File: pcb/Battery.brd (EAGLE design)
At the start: 90 x 15 mm, 18 parts, among them IC1 SN74LVC14APW, X1 MOLEX_1MM_FPC, X2 PVA2OAH11.7NV2, X3 PVA2OAH11.7NV2, X4 PVA2OAH11.7NV2, X5 PVA2OAH11.7NV2

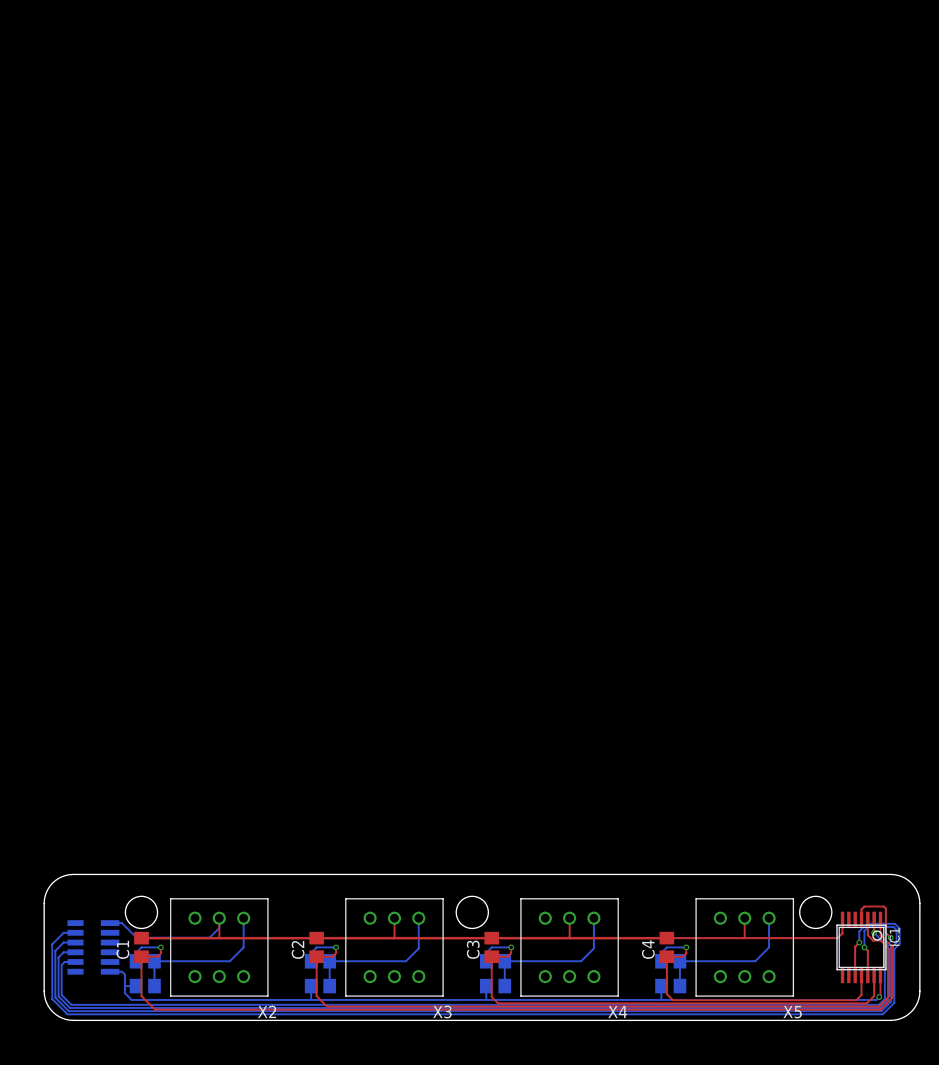
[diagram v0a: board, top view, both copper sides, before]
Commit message: Board dimension created
-reworked schematics
-added PCB for battery-holder
-added PCB for UI
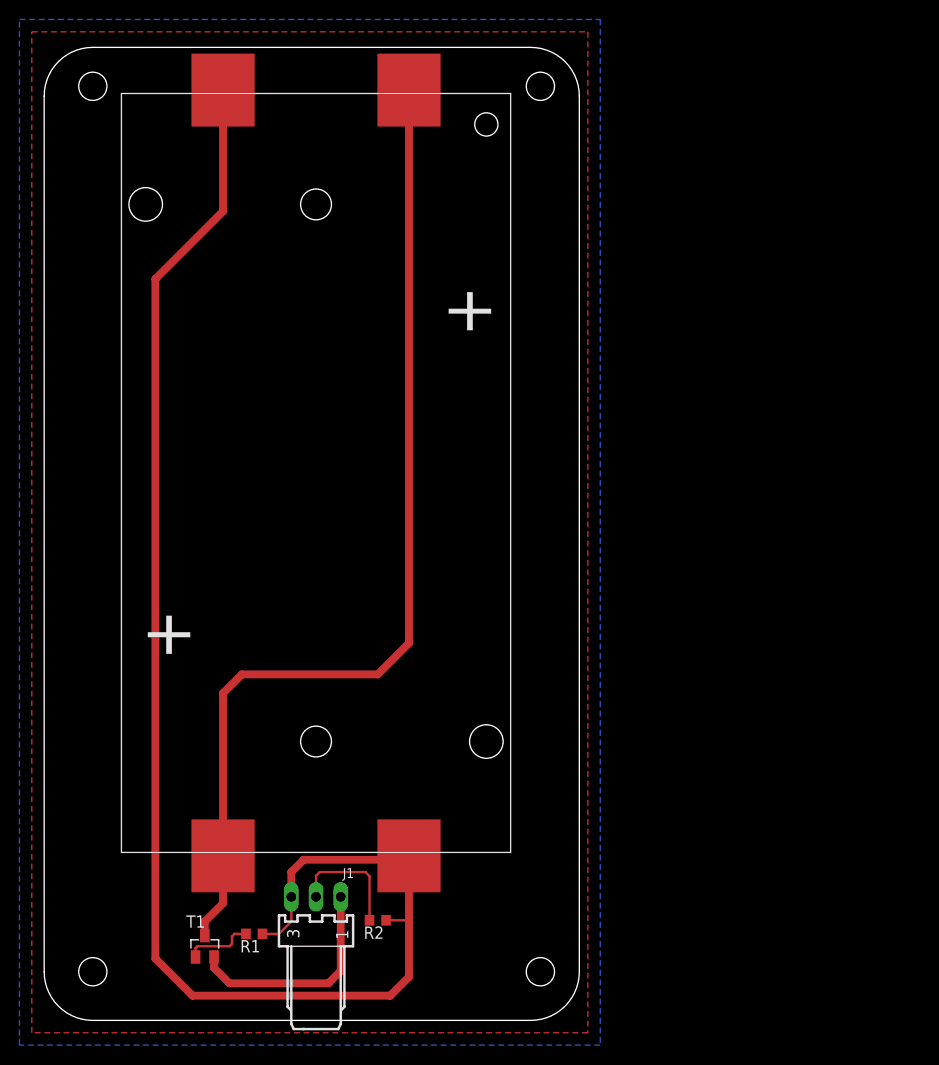
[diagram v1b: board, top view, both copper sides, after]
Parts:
- removed C1, C2, C3, C4: 1µF, rcl:C0805
- removed IC1: SN74LVC14APW, thermo:TSSOP14
- removed R3, R5, R7: 10k, rcl:R0805
- removed R4, R6, R8: 22k, rcl:R0805
- removed X2, X3, X4, X5: PVA2OAH11.7NV2, thermo:BUTTON-2
- added J1: 22-05-7038-03, con-molex:7395-03
- added T1: PMOS, thermo:SOT23
- R1: value 10k -> 100k; device rcl:R0805 -> rcl:R0603
- R2: value 22k -> NTC-0603; device rcl:R0805 -> thermo:R0603
- X1: value MOLEX_1MM_FPC -> LI-ION_BATHOL2; device thermo:1MM_FPC_ZIF -> thermo:HOLDER_2
- moved X1 53.9 mm to (27.9, 56.3), flipped to the top
- moved R2 24.3 mm to (34.3, 10.3), flipped to the top, turned to 180 degrees
- moved R1 12.4 mm to (21.6, 8.89), flipped to the top
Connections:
- removed net +3V3: IC1.14, R1.1, R3.1, R5.1, R7.1, X1.1, X1.7
- removed net N$1: R1.2, R2.1, X2.2
- removed net N$10: R5.2, R6.1, X4.2
- removed net N$11: C3.1, IC1.13, R6.2
- removed net N$12: R7.2, R8.1, X5.2
- removed net N$13: C4.1, IC1.11, R8.2
- removed net N$3: R3.2, R4.1, X3.2
- removed net N$9: C2.1, IC1.3, R4.2
- removed net UI_BUTTON_INT_0: IC1.2, X1.2, X1.8
- removed net UI_BUTTON_INT_1: IC1.4, X1.3, X1.9
- removed net UI_BUTTON_INT_2: IC1.12, X1.10, X1.4
- removed net UI_BUTTON_INT_3: IC1.10, X1.11, X1.5
- new net BAT: J1.1, T1.2
- new net N$4: R1.2, T1.1
- new net NTC: J1.2, R2.2
- net GND: now also J1.3, R1.1, R2.1, X1.2, X1.3; no longer C1.2, C2.2, C3.2, C4.2, IC1.7, X1.12, X1.6, X2.0, X3.0, X4.0, X5.0
- net N$2: now also T1.3, X1.1, X1.4; no longer C1.1, IC1.1, R2.2
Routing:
- net UI_BUTTON_INT_3: track 113.4 -> 0.00 mm, vias 1 -> 0
- net UI_BUTTON_INT_2: track 110.0 -> 0.00 mm, vias 1 -> 0
- net UI_BUTTON_INT_1: track 105.5 -> 0.00 mm, vias 1 -> 0
- net UI_BUTTON_INT_0: track 98.5 -> 0.00 mm, vias 1 -> 0
- net +3V3: track 89.2 -> 0.00 mm, vias 1 -> 0
- net N$9: track 79.5 -> 0.00 mm, vias 1 -> 0
- net GND: track 95.1 -> 156.7 mm
- net N$11: track 52.6 -> 0.00 mm, vias 1 -> 0
- net N$13: track 32.7 -> 0.00 mm, vias 1 -> 0
- net BAT: track 0.00 -> 22.9 mm
- net N$3: track 15.4 -> 0.00 mm
- net N$10: track 15.4 -> 0.00 mm
- net N$1: track 15.3 -> 0.00 mm
- net N$12: track 15.3 -> 0.00 mm
- net NTC: track 0.00 -> 12.5 mm
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- added copper zone on layer 16, net BAT
- added copper zone on layer 1, net GND
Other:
- board size 90 x 15 mm -> 55 x 100 mm
